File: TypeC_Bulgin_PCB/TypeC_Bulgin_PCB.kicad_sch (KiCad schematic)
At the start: 12 parts, among them J1 Conn_01x01_Female, J10 Conn_01x01_Female, J11 Conn_01x01_Female, J12 Conn_01x01_Female, J2 Conn_01x01_Female, J3 USB_C_Receptacle, J4 Conn_01x02_Female, J5 Conn_01x02_Female, J6 Conn_01x02_Female, J7 Conn_01x02_Female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

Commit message: v0.6 connectors prototype were added
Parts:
- removed J10, J11, J12, J9: Conn_01x01_Female, Connector_PinHeader_1.00mm:PinHeader_1x01_P1.00mm_Vertical, symbol Connector:Conn_01x01_Female
- removed J4, J5, J6, J7: Conn_01x02_Female, Connector_PinHeader_1.00mm:PinHeader_1x02_P1.00mm_Vertical, symbol Connector:Conn_01x02_Female
- added J3, J4: Conn_01x13, Connector_Molex:Molex_Picoflex_90325-0014_2x07_P1.27mm_Vertical, symbol Connector_Generic:Conn_01x13
- added J5: Conn_02x10_Odd_Even, Connector_Molex:Molex_Picoflex_90325-0020_2x10_P1.27mm_Vertical, symbol Connector_Generic:Conn_02x10_Odd_Even
- renumbered J3 to J6, J8 to J7
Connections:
- net RX2-: now reaches J6.A10 (RX2-)
- net RX2-: now also J4.12 (Pin_12), J5.15 (Pin_15)
- net RX2+: now reaches J6.A11 (RX2+)
- net RX2+: now also J4.11 (Pin_11), J5.16 (Pin_16)
- net GND: now reaches J6.A1 (GND), J6.A12 (GND), J6.B1 (GND), J6.B12 (GND)
- net GND: now also J3.10 (Pin_10), J3.13 (Pin_13), J3.4 (Pin_4), J3.7 (Pin_7), J4.10 (Pin_10), J4.13 (Pin_13), J4.4 (Pin_4), J4.7 (Pin_7), J5.1 (Pin_1), J5.17 (Pin_17), J5.20 (Pin_20), J5.4 (Pin_4)
- net RX1-: now reaches J6.B10 (RX1-)
- net RX1-: now also J3.12 (Pin_12), J5.2 (Pin_2)
- net RX1+: now reaches J6.B11 (RX1+)
- net RX1+: now also J3.11 (Pin_11), J5.3 (Pin_3)
- net TX1+: now reaches J6.A2 (TX1+)
- net TX1+: now also J3.5 (Pin_5), J5.6 (Pin_6)
- net TX1-: now reaches J6.A3 (TX1-)
- net TX1-: now also J3.6 (Pin_6), J5.5 (Pin_5)
- net TX2+: now reaches J6.B2 (TX2+)
- net TX2+: now also J4.5 (Pin_5), J5.19 (Pin_19)
- net TX2-: now reaches J6.B3 (TX2-)
- net TX2-: now also J4.6 (Pin_6), J5.18 (Pin_18)
- new net VBUS: J3.1 (Pin_1), J3.2 (Pin_2), J4.1 (Pin_1), J4.2 (Pin_2), J5.10 (Pin_10), J5.11 (Pin_11)

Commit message: v0.8 ADT 13 pins was created
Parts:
- removed J2, J7: Conn_01x01_Female, Connector_PinHeader_1.00mm:PinHeader_1x01_P1.00mm_Vertical, symbol Connector:Conn_01x01_Female
- removed J5: Conn_02x10_Odd_Even, Connector_Molex:Molex_Picoflex_90325-0020_2x10_P1.27mm_Vertical, symbol Connector_Generic:Conn_02x10_Odd_Even
- J3, J4: footprint Connector_Molex:Molex_Picoflex_90325-0014_2x07_P1.27mm_Vertical -> TypeC_Bulgin_PCB:ADT_13pin
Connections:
- net VBUS: now also J6.A4 (VBUS), J6.A9 (VBUS), J6.B4 (VBUS), J6.B9 (VBUS)
- now unconnected: J1.1 (Pin_1)
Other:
- moved on the sheet: J3, J4

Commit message: v0.91 circuit was corrected
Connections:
- net RX1+: now also J3.12 (Pin_12); no longer J3.11 (Pin_11)
- net RX1-: now also J3.11 (Pin_11); no longer J3.12 (Pin_12)
- net RX2+: now also J4.12 (Pin_12); no longer J4.11 (Pin_11)
- net RX2-: now also J4.11 (Pin_11); no longer J4.12 (Pin_12)
- net TX1+: now also J6.B2 (TX2+); no longer J6.A2 (TX1+)
- net TX1-: now also J6.B3 (TX2-); no longer J6.A3 (TX1-)
- net TX2+: now also J6.A2 (TX1+); no longer J6.B2 (TX2+)
- net TX2-: now also J6.A3 (TX1-); no longer J6.B3 (TX2-)

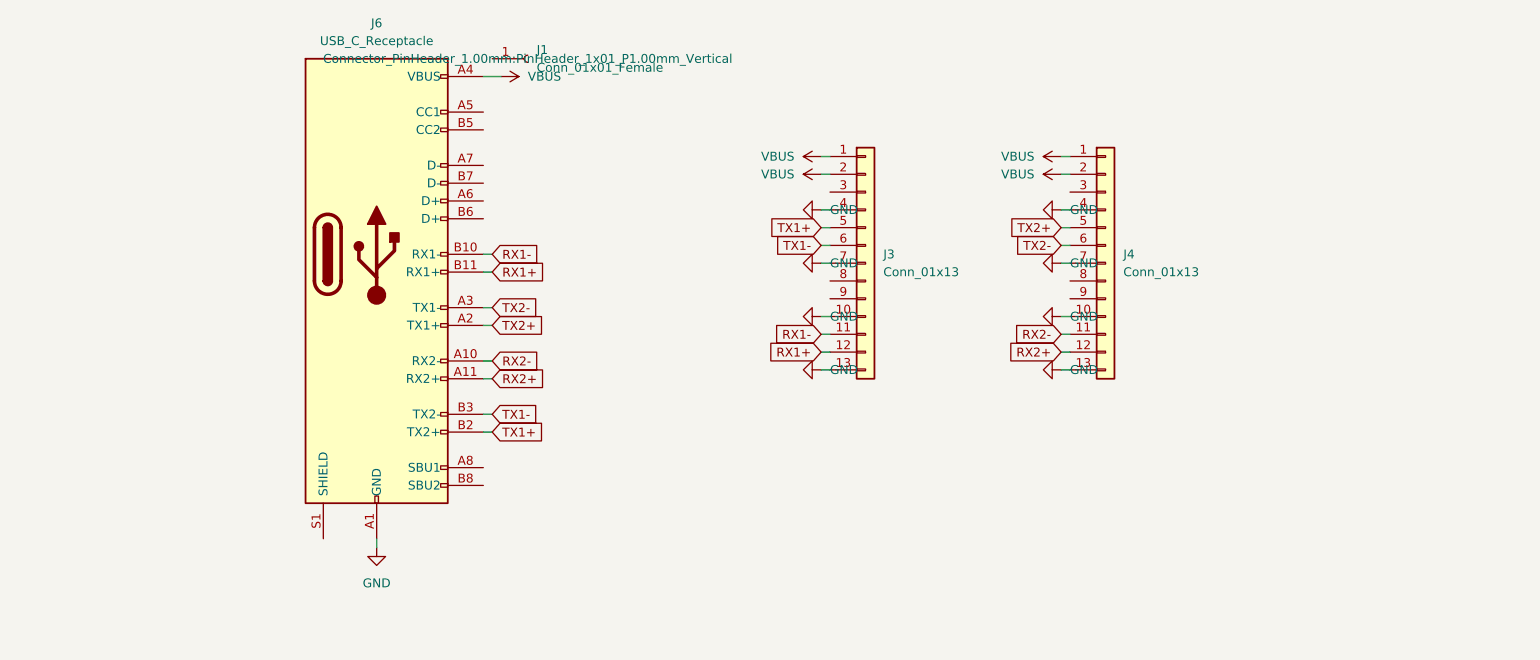
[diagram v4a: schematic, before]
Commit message: v0.95 DRC errors were corrected
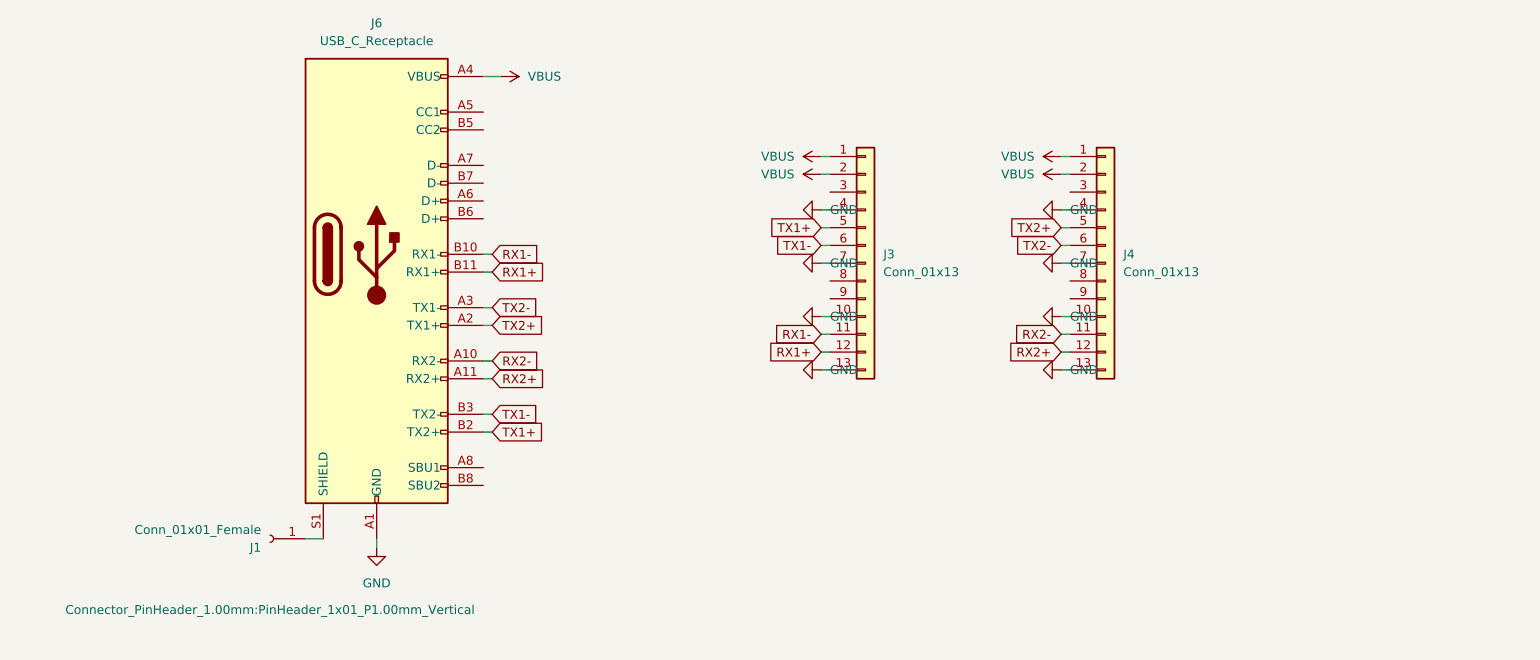
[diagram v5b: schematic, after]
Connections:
- net at J6.S1 (SHIELD): now also J1.1 (Pin_1)
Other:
- moved on the sheet: J1
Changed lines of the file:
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@@
 (kicad_sch (version 20211123) (generator eeschema)
   (paper "A4")
+  (wire (pts (xy 118.11 118.11) (xy 120.65 118.11))
+    (stroke (width 0) (type default) (color 0 0 0 0))
+  )
   (wire (pts (xy 143.51 102.87) (xy 144.78 102.87))
     (stroke (width 0) (type default) (color 0 0 0 0))
@@
     (pin "1")
   )
-  (symbol (lib_id "Connector:Conn_01x01_Female") (at 149.86 49.53 0) (unit 1)
-    (in_bom yes) (on_board yes) (fields_autoplaced)
-    (property "Reference" "J1" (id 0) (at 151.13 48.2599 0)
-      (effects (font (size 1.27 1.27)) (justify left))
-    )
-    (property "Value" "Conn_01x01_Female" (id 1) (at 151.13 50.7999 0)
-      (effects (font (size 1.27 1.27)) (justify left))
-    )
-    (property "Footprint" "Connector_PinHeader_1.00mm:PinHeader_1x01_P1.00mm_Vertical" (id 2) (at 149.86 49.53 0))
-    (property "Datasheet" "~" (id 3) (at 149.86 49.53 0)
-      (effects (font (size 1.27 1.27)) hide)
-    )
+  (symbol (lib_id "Connector:Conn_01x01_Female") (at 113.03 118.11 180) (unit 1)
+    (in_bom yes) (on_board yes)
+    (property "Reference" "J1" (id 0) (at 111.76 119.3801 0)
+      (effects (font (size 1.27 1.27)) (justify left))
+    )
+    (property "Value" "Conn_01x01_Female" (id 1) (at 111.76 116.8401 0)
+      (effects (font (size 1.27 1.27)) (justify left))
+    )
+    (property "Footprint" "Connector_PinHeader_1.00mm:PinHeader_1x01_P1.00mm_Vertical" (id 2) (at 113.03 128.27 0))
+    (property "Datasheet" "~" (id 3) (at 113.03 118.11 0)
+      (effects (font (size 1.27 1.27)) hide)
+    )
